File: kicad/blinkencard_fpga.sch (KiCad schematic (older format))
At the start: 1 part, among them U1 ICE40UP5K-SG48ITR

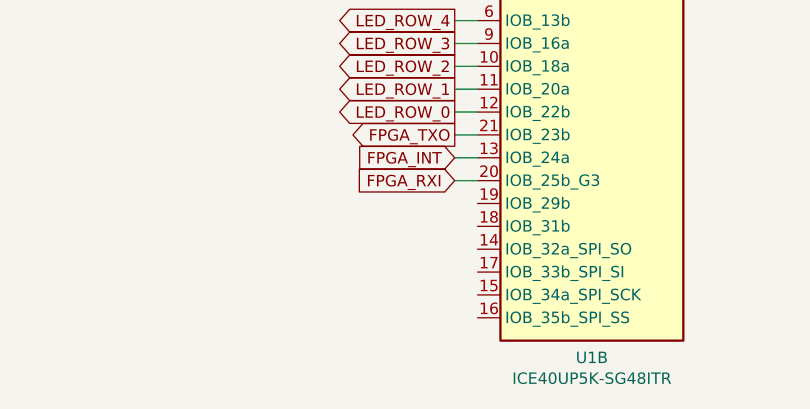
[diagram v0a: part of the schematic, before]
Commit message: Start routing LEDs. Start ESP32 integration
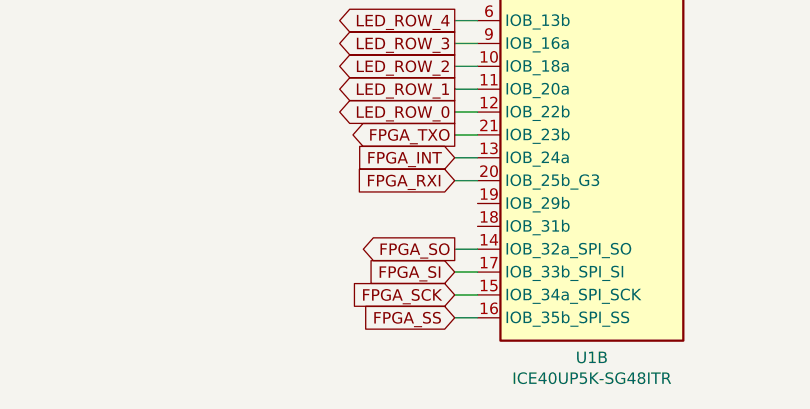
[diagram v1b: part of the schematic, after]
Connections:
- net FPGA_SO: now reaches U1.14 (IOB_32a_SPI_SO)
- net FPGA_SCK: now reaches U1.15 (IOB_34a_SPI_SCK)
- net FPGA_SS: now reaches U1.16 (IOB_35b_SPI_SS)
- net FPGA_SI: now reaches U1.17 (IOB_33b_SPI_SI)
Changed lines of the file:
@@
 Wire Wire Line
 	5550 2700 5550 2800
+Text GLabel 4950 4500 0    50   Output ~ 0
+FPGA_SO
+Text GLabel 4950 4600 0    50   Input ~ 0
+FPGA_SI
+Text GLabel 4950 4700 0    50   Input ~ 0
+FPGA_SCK
+Text GLabel 4950 4800 0    50   Input ~ 0
+FPGA_SS
+Wire Wire Line
+	4950 4500 5050 4500
+Wire Wire Line
+	4950 4600 5050 4600
+Wire Wire Line
+	4950 4700 5050 4700
+Wire Wire Line
+	4950 4800 5050 4800
 $EndSCHEMATC

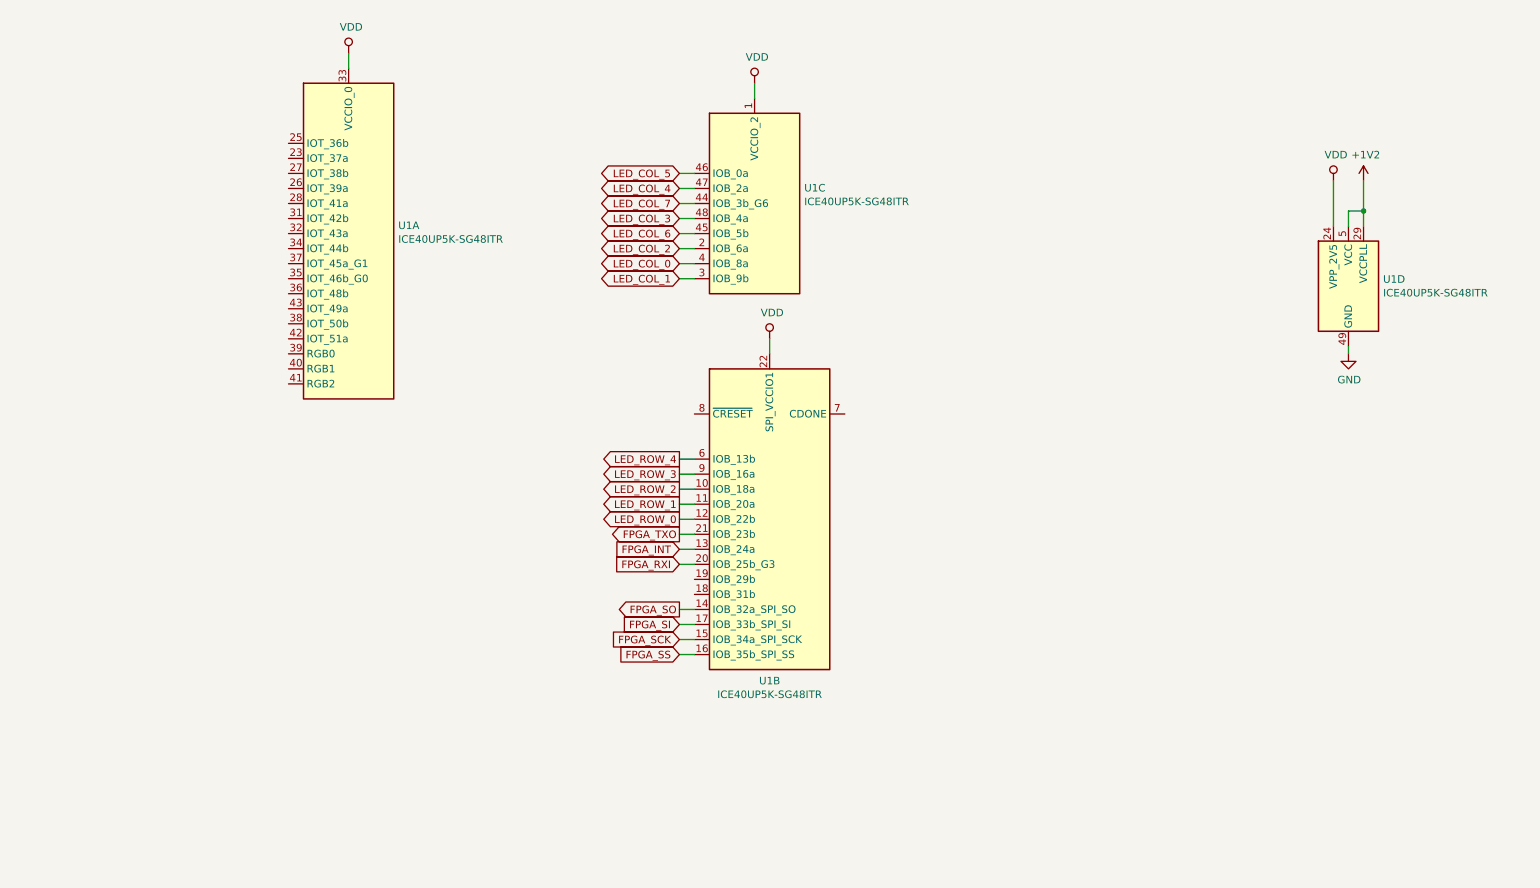
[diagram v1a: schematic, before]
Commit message: Use CP2102A USB-UART and GPIO instead of ESP32 to keep it simple. Add power section and start routing.
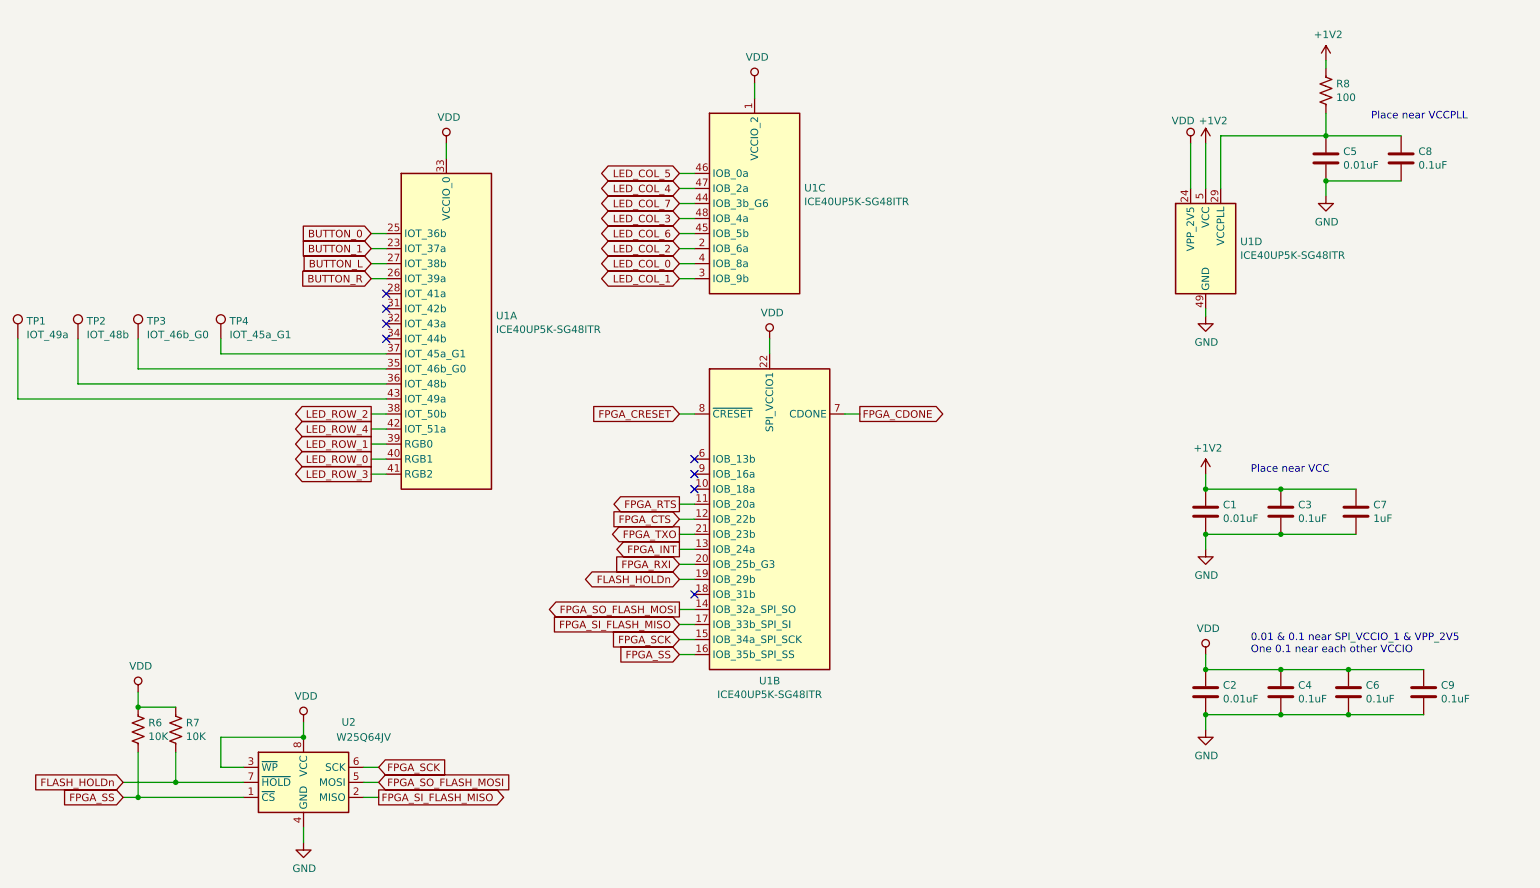
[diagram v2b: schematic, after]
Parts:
- added C1, C2, C5: 0.01uF, Capacitor_SMD:C_0805_2012Metric, symbol Device:C
- added C3, C4, C6, C8, C9: 0.1uF, Capacitor_SMD:C_0805_2012Metric, symbol Device:C
- added C7: 1uF, Capacitor_SMD:C_0805_2012Metric, symbol Device:C
- added R6, R7: 10K, Resistor_SMD:R_0603_1608Metric, symbol Device:R_US
- added R8: 100, Resistor_SMD:R_0603_1608Metric, symbol Device:R_US
- added TP1: IOT_49a, TestPoint:TestPoint_Pad_D1.5mm, symbol Connector:TestPoint
- added TP2: IOT_48b, TestPoint:TestPoint_Pad_D1.5mm, symbol Connector:TestPoint
- added TP3: IOT_46b_G0, TestPoint:TestPoint_Pad_D1.5mm, symbol Connector:TestPoint
- added TP4: IOT_45a_G1, TestPoint:TestPoint_Pad_D1.5mm, symbol Connector:TestPoint
- added U2: W25Q64JV, Package_SO:SOIC-8_5.23x5.23mm_P1.27mm, symbol Memory_EEPROM:25LCxxx
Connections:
- net +1V2: now also C1.1, C3.1, C7.1, R8.1; no longer U1.29 (VCCPLL)
- net FPGA_SCK: now also U2.6 (SCK)
- net FPGA_SS: now also R6.2, U2.1 (~CS)
- net GND: now also C1.2, C2.2, C3.2, C4.2, C5.2, C6.2, C7.2, C8.2, C9.2, U2.4 (GND)
- net LED_ROW_0: now also U1.40 (RGB1); no longer U1.12 (IOB_22b)
- net LED_ROW_1: now also U1.39 (RGB0); no longer U1.11 (IOB_20a)
- net LED_ROW_2: now also U1.38 (IOT_50b); no longer U1.10 (IOB_18a)
- net LED_ROW_3: now also U1.41 (RGB2); no longer U1.9 (IOB_16a)
- net LED_ROW_4: now also U1.42 (IOT_51a); no longer U1.6 (IOB_13b)
- net VDD: now also C2.1, C4.1, C6.1, C9.1, R6.1, R7.1, U2.3 (~WP), U2.8 (VCC)
- net BUTTON_1: now reaches U1.23 (IOT_37a)
- net BUTTON_0: now reaches U1.25 (IOT_36b)
- net BUTTON_R: now reaches U1.26 (IOT_39a)
- net BUTTON_L: now reaches U1.27 (IOT_38b)
- net at U1.35 (IOT_46b_G0): now also TP3.1
- net at U1.36 (IOT_48b): now also TP2.1
- net at U1.37 (IOT_45a_G1): now also TP4.1
- net at U1.43 (IOT_49a): now also TP1.1
- net FLASH_HOLDn: now reaches U1.19 (IOB_29b)
- net FLASH_HOLDn: now also R7.2, U2.7 (~HOLD)
- net FPGA_CDONE: now reaches U1.7 (CDONE)
- net FPGA_CRESET: now reaches U1.8 (~CRESET)
- net FPGA_SI renamed FPGA_SI_FLASH_MISO
- net FPGA_SI_FLASH_MISO: now also U2.2 (MISO)
- net FPGA_SO renamed FPGA_SO_FLASH_MOSI
- net FPGA_SO_FLASH_MOSI: now also U2.5 (MOSI)
- new net: C5.1, C8.1, R8.2, U1.29 (VCCPLL)
- new net FPGA_CTS: U1.12 (IOB_22b)
- new net FPGA_RTS: U1.11 (IOB_20a)
- no-connect marks 0 -> 8
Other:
- note added: "0.01 & 0.1 near SPI_VCCIO_1 & VPP_2V5\nOne 0.1 near each other VCCIO"
- note added: "Place near VCC"
- note added: "Place near VCCPLL"
- moved on the sheet: U1A, U1D

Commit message: LED routing
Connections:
- net LED_ROW_0: now also U1.41 (RGB2); no longer U1.40 (RGB1)
- net LED_ROW_1: now also U1.40 (RGB1); no longer U1.39 (RGB0)
- net LED_ROW_2: now also U1.39 (RGB0); no longer U1.38 (IOT_50b)
- net LED_ROW_3: now also U1.38 (IOT_50b); no longer U1.41 (RGB2)
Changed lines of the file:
@@
 	1    0    0    -1
 $EndComp
-Text GLabel 2900 3500 0    50   Output ~ 0
+Text GLabel 2900 3600 0    50   Output ~ 0
 LED_ROW_0
 Text GLabel 2900 3400 0    50   Output ~ 0
-LED_ROW_1
+LED_ROW_2
 Text GLabel 2900 3200 0    50   Output ~ 0
-LED_ROW_2
-Text GLabel 2900 3600 0    50   Output ~ 0
 LED_ROW_3
-Text GLabel 2900 3300 0    50   Output ~ 0
-LED_ROW_4
 Wire Wire Line
 	3000 3200 2900 3200
@@
 	1    0    0    -1
 $EndComp
+Text GLabel 2900 3500 0    50   Output ~ 0
+LED_ROW_1
+Text GLabel 2900 3300 0    50   Output ~ 0
+LED_ROW_4
 $EndSCHEMATC

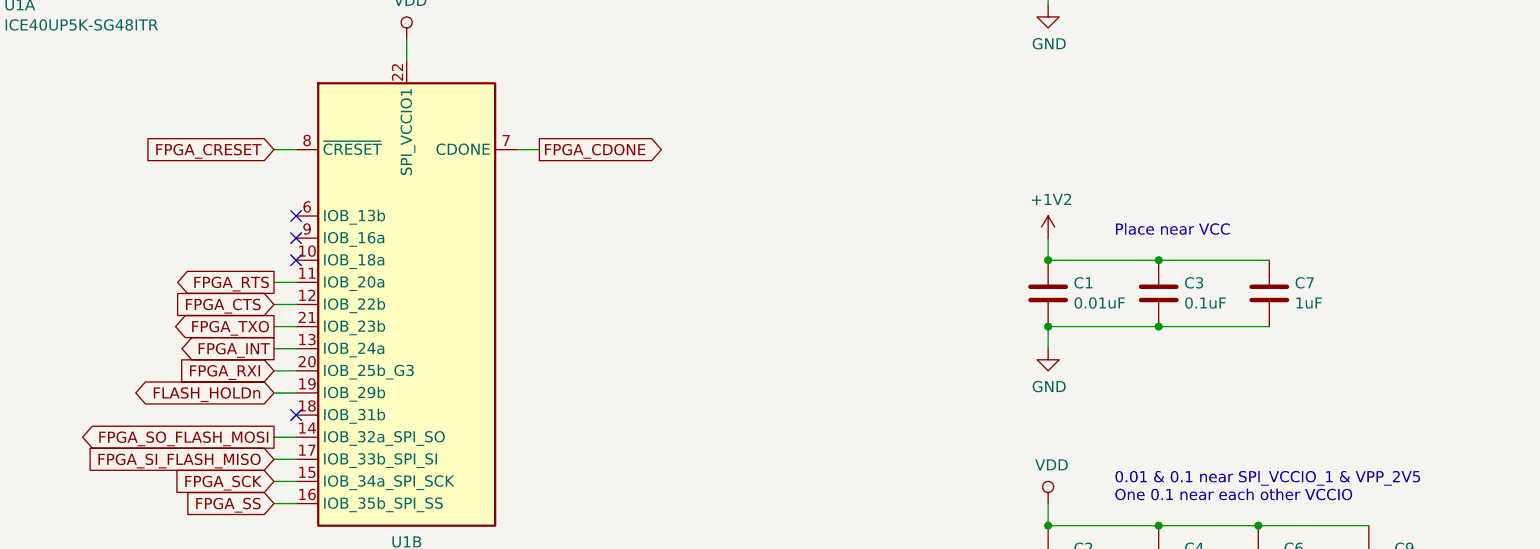
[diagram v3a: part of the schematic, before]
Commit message: Mostly routed
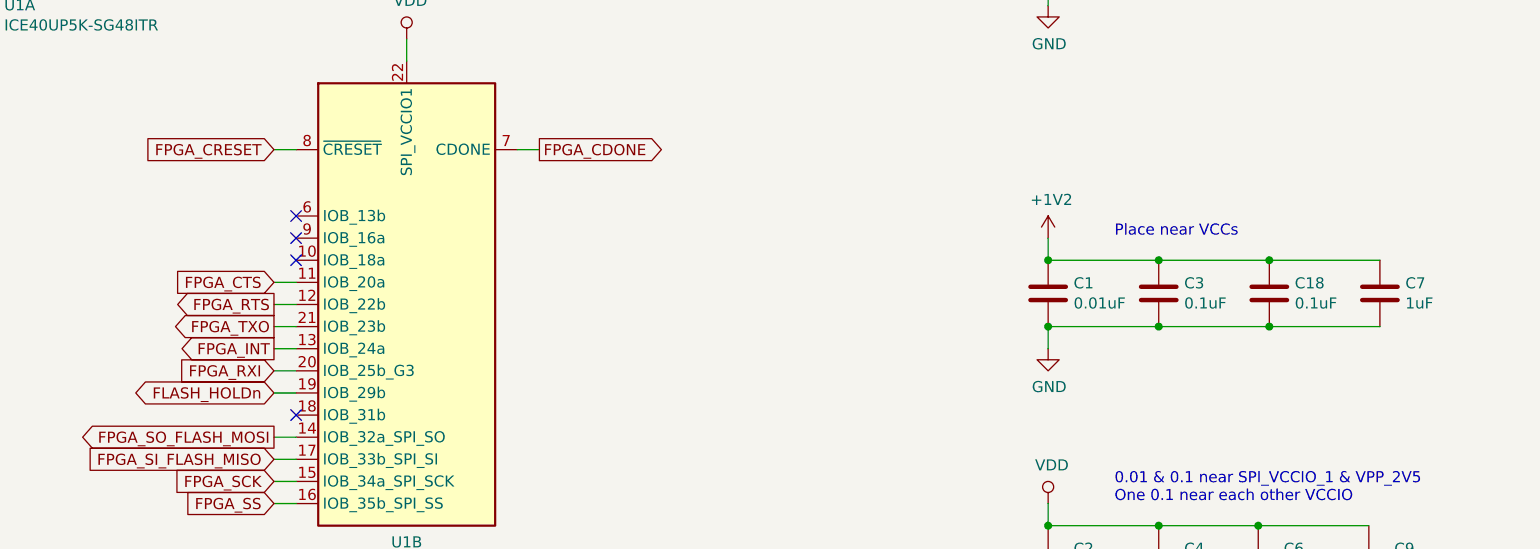
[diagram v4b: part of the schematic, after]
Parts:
- added C18: 0.1uF, Capacitor_SMD:C_0805_2012Metric, symbol Device:C
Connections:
- net +1V2: now also C18.1
- net FPGA_CTS: now also U1.11 (IOB_20a); no longer U1.12 (IOB_22b)
- net FPGA_RTS: now also U1.12 (IOB_22b); no longer U1.11 (IOB_20a)
- net GND: now also C18.2
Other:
- note added: "Place near VCCs"
- note removed: "Place near VCC"
- moved on the sheet: C7
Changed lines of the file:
@@
 L Device:C C7
 U 1 1 5DD3A06D
-P 9450 3850
-F 0 "C7" H 9565 3896 50  0000 L CNN
-F 1 "1uF" H 9565 3805 50  0000 L CNN
-F 2 "Capacitor_SMD:C_0805_2012Metric" H 9488 3700 50  0001 C CNN
-F 3 "~" H 9450 3850 50  0001 C CNN
-	1    9450 3850
+P 9950 3850
+F 0 "C7" H 10065 3896 50  0000 L CNN
+F 1 "1uF" H 10065 3805 50  0000 L CNN
+F 2 "Capacitor_SMD:C_0805_2012Metric" H 9988 3700 50  0001 C CNN
+F 3 "~" H 9950 3850 50  0001 C CNN
+	1    9950 3850
 	1    0    0    -1
 $EndComp
@@
 0.01 & 0.1 near SPI_VCCIO_1 & VPP_2V5\nOne 0.1 near each other VCCIO
 Text Notes 8750 3600 0    50   ~ 0
-Place near VCC
+Place near VCCs
 Text Notes 9550 1250 0    50   ~ 0
 Place near VCCPLL
@@
 Wire Wire Line
 	550  3100 3000 3100
-Text GLabel 4950 3800 0    50   Output ~ 0
+Text GLabel 4950 3900 0    50   Output ~ 0
 FPGA_RTS
-Text GLabel 4950 3900 0    50   Input ~ 0
+Text GLabel 4950 3800 0    50   Input ~ 0
 FPGA_CTS
 Wire Wire Line
@@
 Text GLabel 2900 3300 0    50   Output ~ 0
 LED_ROW_4
+$Comp
+L Device:C C18
+U 1 1 5DDB0604
+P 9450 3850
+F 0 "C18" H 9565 3896 50  0000 L CNN
+F 1 "0.1uF" H 9565 3805 50  0000 L CNN
+F 2 "Capacitor_SMD:C_0805_2012Metric" H 9488 3700 50  0001 C CNN
+F 3 "~" H 9450 3850 50  0001 C CNN
+	1    9450 3850
+	1    0    0    -1
+$EndComp
+Wire Wire Line
+	9450 3700 9950 3700
+Connection ~ 9450 3700
+Wire Wire Line
+	9950 4000 9450 4000
+Connection ~ 9450 4000
 $EndSCHEMATC
